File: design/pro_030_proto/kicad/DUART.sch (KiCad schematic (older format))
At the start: 27 parts, among them IC2 XR68C681CJTR-F-XR68C681, J1 Conn_01x06_Male, J2 Conn_01x06_Male, J3 Conn_02x08_Odd_Even, Y1 3.6864MHz

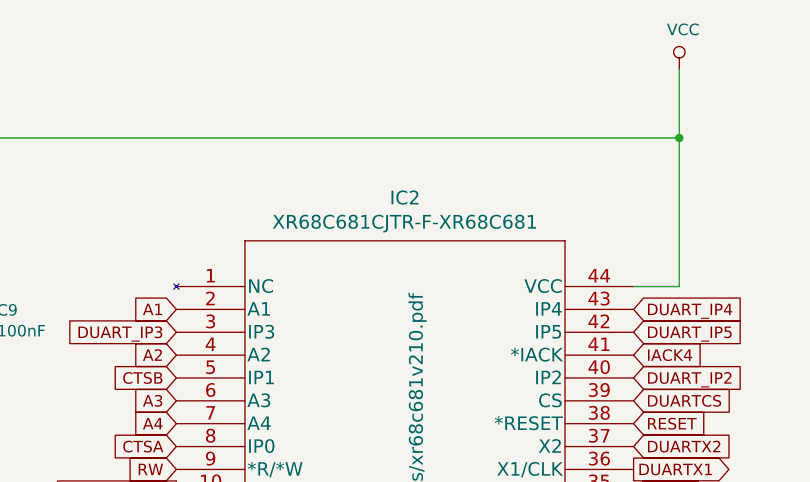
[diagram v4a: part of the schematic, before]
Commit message: Add IO and XVID glue etc.
* Add IO Select glue
* Add Xosera glue
* Add new glues to schematic
* Clean up libs
* Reannotate (again)
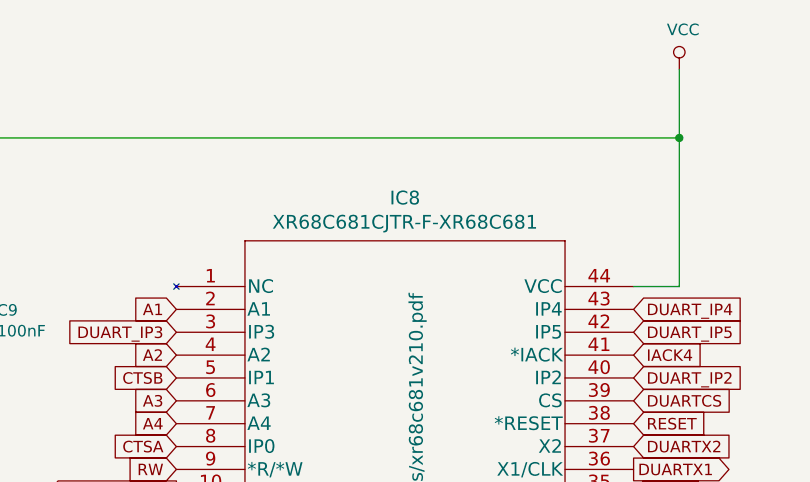
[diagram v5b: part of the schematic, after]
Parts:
- renumbered IC2 to IC8
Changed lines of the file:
@@
 $EndDescr
 $Comp
-L rosco_m68k:XR68C681CJTR-F-XR68C681 IC2
+L rosco_m68k:XR68C681CJTR-F-XR68C681 IC8
 U 1 1 60FBD731
 P 2000 1850
-F 0 "IC2" H 3000 2237 60  0000 C CNN
+F 0 "IC8" H 3000 2237 60  0000 C CNN
 F 1 "XR68C681CJTR-F-XR68C681" H 3000 2131 60  0000 C CNN
 F 2 "Package_LCC:PLCC-44_THT-Socket" H 3000 2090 60  0001 C CNN

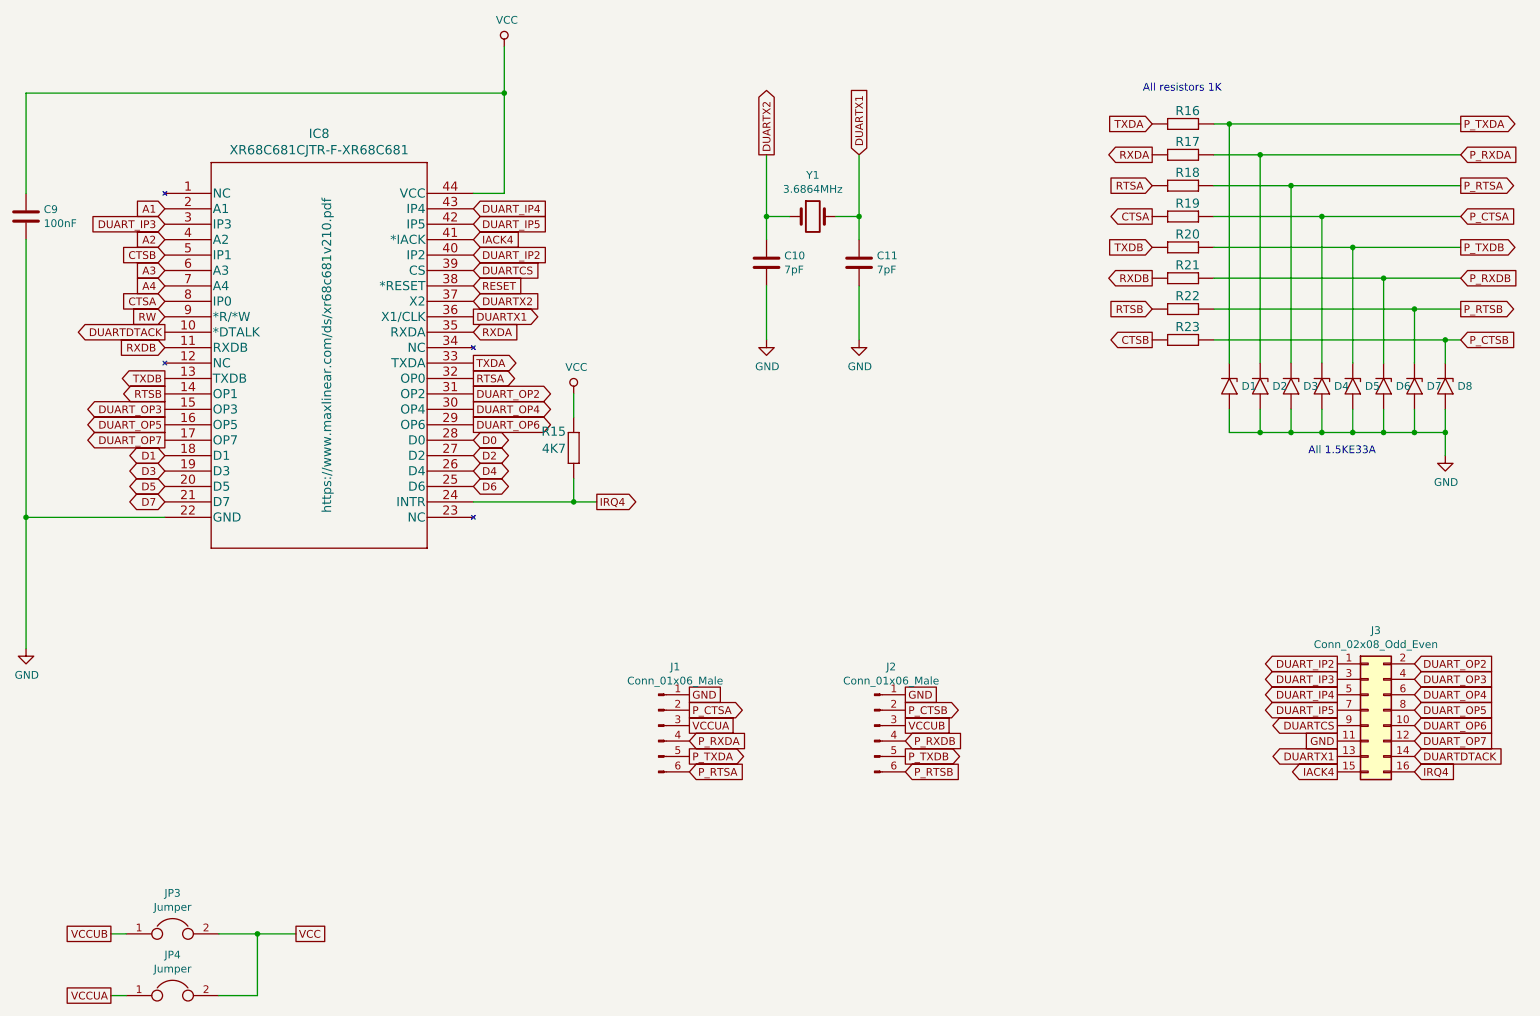
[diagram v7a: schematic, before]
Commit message: Fix DUART DTACK SNAFU
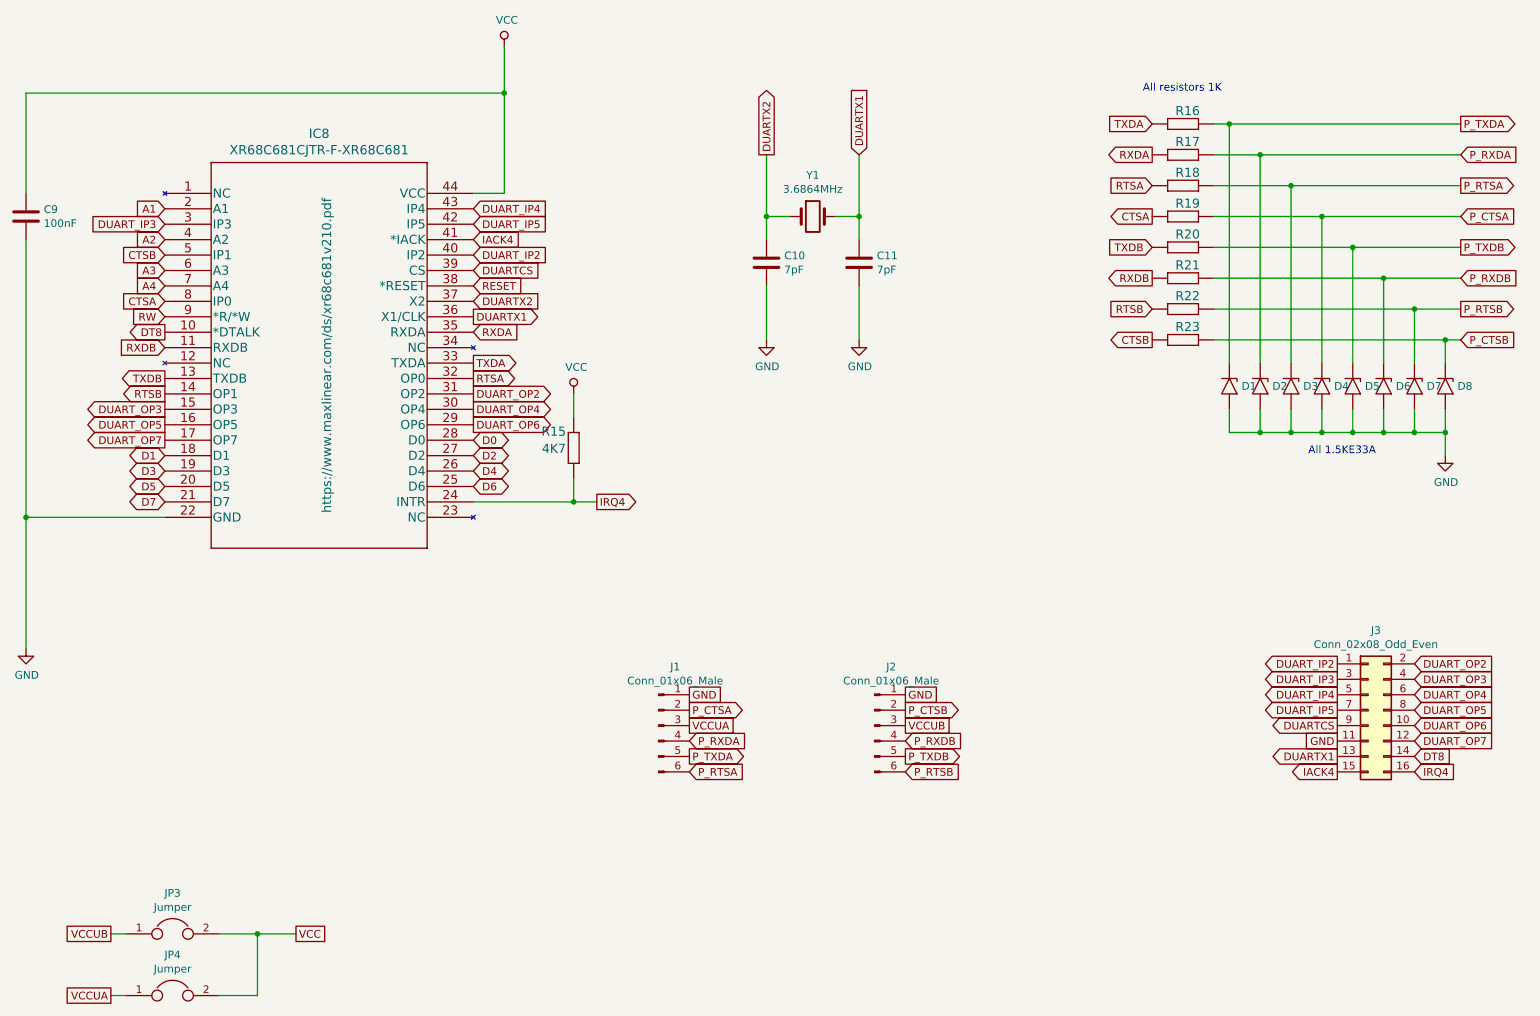
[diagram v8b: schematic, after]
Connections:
- net DUARTDTACK renamed DT8
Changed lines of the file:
@@
 RTSA
 Text GLabel 2000 2750 0    50   Output ~ 0
-DUARTDTACK
+DT8
 Text GLabel 4800 3850 2    50   Output ~ 0
 IRQ4
@@
 DUARTCS
 Text GLabel 10100 5500 2    50   Input ~ 0
-DUARTDTACK
+DT8
 Text GLabel 10100 5600 2    50   Input ~ 0
 IRQ4
